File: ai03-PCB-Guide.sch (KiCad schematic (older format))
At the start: 4 parts

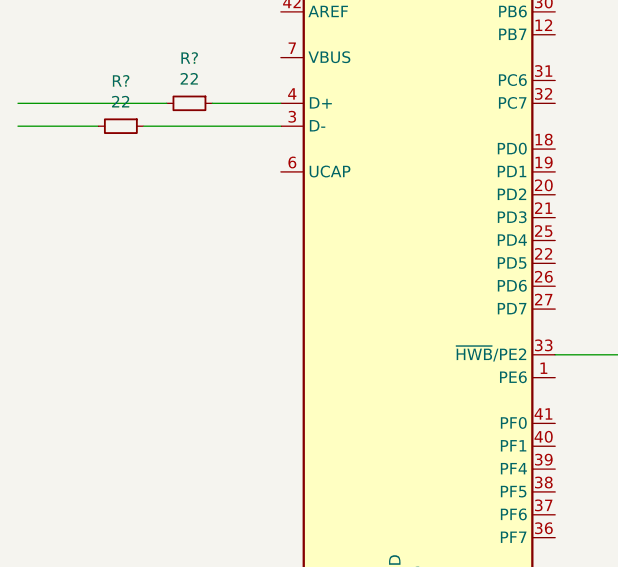
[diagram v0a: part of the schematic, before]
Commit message: New Capacitor
Added the first capacitor to the board. Done by following the official documentation and the tutorial. Generally speaking it's good if you can find the official documentation and some form of proven use case provided by another production team. (In this case, TEENSY)
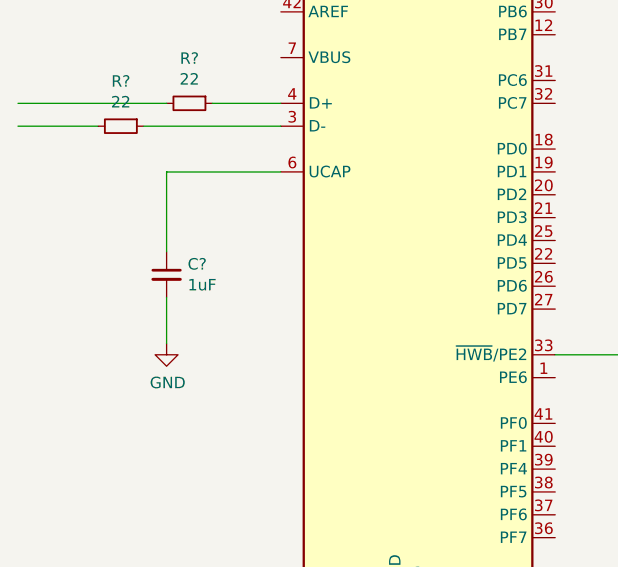
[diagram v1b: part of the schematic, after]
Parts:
- added C?: 1uF, symbol Device:C_Small
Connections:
- wire segments 11 -> 14
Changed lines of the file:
@@
 Wire Wire Line
 	2050 3100 1400 3100
+$Comp
+L Device:C_Small C?
+U 1 1 5EEF2142
+P 2050 3850
+F 0 "C?" H 2142 3896 50  0000 L CNN
+F 1 "1uF" H 2142 3805 50  0000 L CNN
+F 2 "" H 2050 3850 50  0001 C CNN
+F 3 "~" H 2050 3850 50  0001 C CNN
+	1    2050 3850
+	1    0    0    -1
+$EndComp
+Wire Wire Line
+	2550 3400 2050 3400
+Wire Wire Line
+	2050 3400 2050 3750
+$Comp
+L power:GND #PWR?
+U 1 1 5EEF42F1
+P 2050 4150
+F 0 "#PWR?" H 2050 3900 50  0001 C CNN
+F 1 "GND" H 2055 3977 50  0000 C CNN
+F 2 "" H 2050 4150 50  0001 C CNN
+F 3 "" H 2050 4150 50  0001 C CNN
+	1    2050 4150
+	1    0    0    -1
+$EndComp
+Wire Wire Line
+	2050 4150 2050 3950
 $EndSCHEMATC

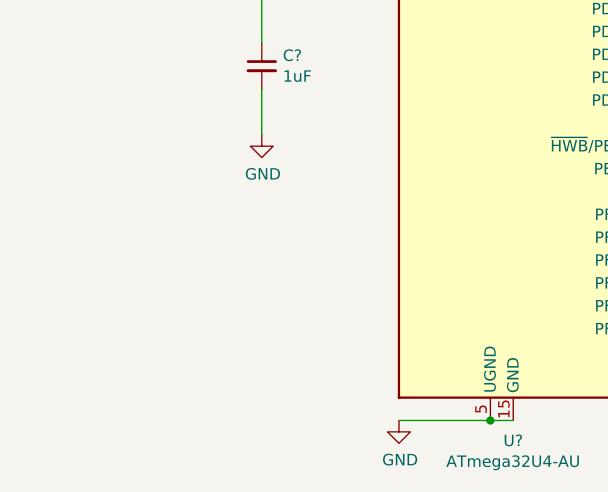
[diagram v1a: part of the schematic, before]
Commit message: Decoupling Capacitors
This step involved making the capacitors that filter the electrical noise from the microcrontroller. The official documentation says to use 0.1uF by each VCC, which would make 4, and a 10uF overall. But when looking at the Teensy Schematic, it uses 3 0.1uF and 1 1uF. The guide says to combine both, and it still works functionally. so that is what has been added here.
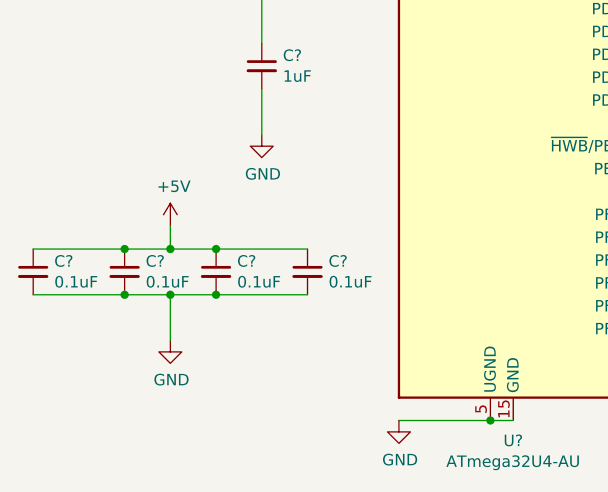
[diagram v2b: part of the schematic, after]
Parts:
- added C? (x4): 0.1uF, symbol Device:C_Small
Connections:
- wire segments 14 -> 24
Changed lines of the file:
@@
 Wire Wire Line
 	2050 4150 2050 3950
+$Comp
+L Device:C_Small C?
+U 1 1 5EEF5F01
+P 1050 4750
+F 0 "C?" H 1142 4796 50  0000 L CNN
+F 1 "0.1uF" H 1142 4705 50  0000 L CNN
+F 2 "" H 1050 4750 50  0001 C CNN
+F 3 "~" H 1050 4750 50  0001 C CNN
+	1    1050 4750
+	1    0    0    -1
+$EndComp
+$Comp
+L Device:C_Small C?
+U 1 1 5EEF6CAE
+P 1450 4750
+F 0 "C?" H 1542 4796 50  0000 L CNN
+F 1 "0.1uF" H 1542 4705 50  0000 L CNN
+F 2 "" H 1450 4750 50  0001 C CNN
+F 3 "~" H 1450 4750 50  0001 C CNN
+	1    1450 4750
+	1    0    0    -1
+$EndComp
+$Comp
+L Device:C_Small C?
+U 1 1 5EEF796E
+P 1850 4750
+F 0 "C?" H 1942 4796 50  0000 L CNN
+F 1 "0.1uF" H 1942 4705 50  0000 L CNN
+F 2 "" H 1850 4750 50  0001 C CNN
+F 3 "~" H 1850 4750 50  0001 C CNN
+	1    1850 4750
+	1    0    0    -1
+$EndComp
+$Comp
+L Device:C_Small C?
+U 1 1 5EEF8927
+P 2250 4750
+F 0 "C?" H 2342 4796 50  0000 L CNN
+F 1 "0.1uF" H 2342 4705 50  0000 L CNN
+F 2 "" H 2250 4750 50  0001 C CNN
+F 3 "~" H 2250 4750 50  0001 C CNN
+	1    2250 4750
+	1    0    0    -1
+$EndComp
+$Comp
+L power:GND #PWR?
+U 1 1 5EEF9C1D
+P 1650 5050
+F 0 "#PWR?" H 1650 4800 50  0001 C CNN
+F 1 "GND" H 1655 4877 50  0000 C CNN
+F 2 "" H 1650 5050 50  0001 C CNN
+F 3 "" H 1650 5050 50  0001 C CNN
+	1    1650 5050
+	1    0    0    -1
+$EndComp
+$Comp
+L power:+5V #PWR?
+U 1 1 5EEFAA60
+P 1650 4550
+F 0 "#PWR?" H 1650 4400 50  0001 C CNN
+F 1 "+5V" H 1665 4723 50  0000 C CNN
+F 2 "" H 1650 4550 50  0001 C CNN
+F 3 "" H 1650 4550 50  0001 C CNN
+	1    1650 4550
+	1    0    0    -1
+$EndComp
+Connection ~ 1850 4650
+Connection ~ 1850 4850
+Connection ~ 1450 4650
+Connection ~ 1450 4850
+Wire Wire Line
+	1450 4850 1650 4850
+Wire Wire Line
+	1450 4650 1650 4650
+Wire Wire Line
+	1650 5050 1650 4850
+Connection ~ 1650 4850
+Wire Wire Line
+	1650 4850 1850 4850
+Wire Wire Line
+	1650 4550 1650 4650
+Connection ~ 1650 4650
+Wire Wire Line
+	1650 4650 1850 4650
+Wire Wire Line
+	1050 4650 1450 4650
+Wire Wire Line
+	1050 4850 1450 4850
+Wire Wire Line
+	1850 4850 2250 4850
+Wire Wire Line
+	1850 4650 2250 4650
 $EndSCHEMATC

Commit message: Crystals and Reset
Added the crystals and routed to GND, also added the Reset button to allow the MCU to be put into bootloader.mm
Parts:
- added C? (x2): 22pF, symbol Device:C_Small
- added SW?: SW_Push, symbol Switch:SW_Push
- added Y?: 16MHz, symbol Device:Crystal_GND24_Small
- C?: value 0.1uF -> 10uF
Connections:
- wire segments 24 -> 44
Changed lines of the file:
@@
 P 2250 4750
 F 0 "C?" H 2342 4796 50  0000 L CNN
-F 1 "0.1uF" H 2342 4705 50  0000 L CNN
+F 1 "10uF" H 2342 4705 50  0000 L CNN
 F 2 "" H 2250 4750 50  0001 C CNN
 F 3 "~" H 2250 4750 50  0001 C CNN
@@
 Wire Wire Line
 	1850 4650 2250 4650
+Wire Wire Line
+	2550 2900 1900 2900
+$Comp
+L power:+5V #PWR?
+U 1 1 5EF047D9
+P 1900 2900
+F 0 "#PWR?" H 1900 2750 50  0001 C CNN
+F 1 "+5V" H 1915 3073 50  0000 C CNN
+F 2 "" H 1900 2900 50  0001 C CNN
+F 3 "" H 1900 2900 50  0001 C CNN
+	1    1900 2900
+	1    0    0    -1
+$EndComp
+$Comp
+L Device:Crystal_GND24_Small Y?
+U 1 1 5EF054D7
+P 2100 2400
+F 0 "Y?" V 2054 2544 50  0000 L CNN
+F 1 "16MHz" V 2145 2544 50  0000 L CNN
+F 2 "" H 2100 2400 50  0001 C CNN
+F 3 "~" H 2100 2400 50  0001 C CNN
+	1    2100 2400
+	0    1    1    0
+$EndComp
+Wire Wire Line
+	2550 2300 2100 2300
+Wire Wire Line
+	2550 2500 2100 2500
+$Comp
+L Device:C_Small C?
+U 1 1 5EF072F6
+P 1700 2200
+F 0 "C?" V 1471 2200 50  0000 C CNN
+F 1 "22pF" V 1562 2200 50  0000 C CNN
+F 2 "" H 1700 2200 50  0001 C CNN
+F 3 "~" H 1700 2200 50  0001 C CNN
+	1    1700 2200
+	0    1    1    0
+$EndComp
+$Comp
+L Device:C_Small C?
+U 1 1 5EF08CB4
+P 1700 2550
+F 0 "C?" V 1471 2550 50  0000 C CNN
+F 1 "22pF" V 1562 2550 50  0000 C CNN
+F 2 "" H 1700 2550 50  0001 C CNN
+F 3 "~" H 1700 2550 50  0001 C CNN
+	1    1700 2550
+	0    1    1    0
+$EndComp
+$Comp
+L power:GND #PWR?
+U 1 1 5EF09377
+P 1550 2750
+F 0 "#PWR?" H 1550 2500 50  0001 C CNN
+F 1 "GND" H 1555 2577 50  0000 C CNN
+F 2 "" H 1550 2750 50  0001 C CNN
+F 3 "" H 1550 2750 50  0001 C CNN
+	1    1550 2750
+	1    0    0    -1
+$EndComp
+Wire Wire Line
+	2100 2300 1800 2300
+Wire Wire Line
+	1800 2300 1800 2200
+Connection ~ 2100 2300
+Wire Wire Line
+	1600 2200 1600 2550
+Wire Wire Line
+	1600 2550 1550 2550
+Wire Wire Line
+	1550 2550 1550 2700
+Connection ~ 1600 2550
+Wire Wire Line
+	1800 2550 2100 2550
+Wire Wire Line
+	2100 2550 2100 2500
+Connection ~ 2100 2500
+Wire Wire Line
+	2000 2400 1950 2400
+Wire Wire Line
+	1950 2400 1950 2600
+Wire Wire Line
+	1950 2600 2200 2600
+Wire Wire Line
+	2200 2600 2200 2400
+Wire Wire Line
+	1950 2600 1800 2600
+Wire Wire Line
+	1800 2600 1800 2700
+Wire Wire Line
+	1800 2700 1550 2700
+Connection ~ 1950 2600
+Connection ~ 1550 2700
+Wire Wire Line
+	1550 2700 1550 2750
+$Comp
+L power:GND #PWR?
+U 1 1 5EF0F3DA
+P 2050 2050
+F 0 "#PWR?" H 2050 1800 50  0001 C CNN
+F 1 "GND" H 2055 1877 50  0000 C CNN
+F 2 "" H 2050 2050 50  0001 C CNN
+F 3 "" H 2050 2050 50  0001 C CNN
+	1    2050 2050
+	1    0    0    -1
+$EndComp
+$Comp
+L Switch:SW_Push SW?
+U 1 1 5EF0FCB2
+P 2350 2100
+F 0 "SW?" H 2350 2385 50  0000 C CNN
+F 1 "SW_Push" H 2350 2294 50  0000 C CNN
+F 2 "" H 2350 2300 50  0001 C CNN
+F 3 "~" H 2350 2300 50  0001 C CNN
+	1    2350 2100
+	1    0    0    -1
+$EndComp
+Wire Wire Line
+	2050 2050 2150 2050
+Wire Wire Line
+	2150 2050 2150 2100
 $EndSCHEMATC

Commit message: AREF Pin and Nets
Added the AREF pin to the Reset. Also added pins to the USB (Ctrl+H allows for this) in order to make it so that I don't have to run wires across the entire schematic when moving past the MCU work.
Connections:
- net labels added: D+, D-
- wire segments 44 -> 49
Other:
- moved on the sheet: SW?
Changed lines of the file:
@@
 L power:GND #PWR?
 U 1 1 5EF0F3DA
-P 2050 2050
-F 0 "#PWR?" H 2050 1800 50  0001 C CNN
-F 1 "GND" H 2055 1877 50  0000 C CNN
-F 2 "" H 2050 2050 50  0001 C CNN
-F 3 "" H 2050 2050 50  0001 C CNN
-	1    2050 2050
+P 1900 2050
+F 0 "#PWR?" H 1900 1800 50  0001 C CNN
+F 1 "GND" H 1905 1877 50  0000 C CNN
+F 2 "" H 1900 2050 50  0001 C CNN
+F 3 "" H 1900 2050 50  0001 C CNN
+	1    1900 2050
 	1    0    0    -1
 $EndComp
@@
 L Switch:SW_Push SW?
 U 1 1 5EF0FCB2
-P 2350 2100
-F 0 "SW?" H 2350 2385 50  0000 C CNN
-F 1 "SW_Push" H 2350 2294 50  0000 C CNN
-F 2 "" H 2350 2300 50  0001 C CNN
-F 3 "~" H 2350 2300 50  0001 C CNN
-	1    2350 2100
+P 2250 2100
+F 0 "SW?" H 2250 2385 50  0000 C CNN
+F 1 "SW_Push" H 2250 2294 50  0000 C CNN
+F 2 "" H 2250 2300 50  0001 C CNN
+F 3 "~" H 2250 2300 50  0001 C CNN
+	1    2250 2100
 	1    0    0    -1
 $EndComp
 Wire Wire Line
-	2050 2050 2150 2050
+	2150 2050 2150 2100
 Wire Wire Line
-	2150 2050 2150 2100
+	2050 2100 2000 2100
+Wire Wire Line
+	2000 2100 2000 2050
+Wire Wire Line
+	2000 2050 1900 2050
+Wire Wire Line
+	2450 2100 2500 2100
+Wire Wire Line
+	2500 1800 2500 2100
+Connection ~ 2500 2100
+Wire Wire Line
+	2500 2100 2550 2100
+$Comp
+L power:+5V #PWR?
+U 1 1 5EF18A9D
+P 2500 1800
+F 0 "#PWR?" H 2500 1650 50  0001 C CNN
+F 1 "+5V" H 2515 1973 50  0000 C CNN
+F 2 "" H 2500 1800 50  0001 C CNN
+F 3 "" H 2500 1800 50  0001 C CNN
+	1    2500 1800
+	1    0    0    -1
+$EndComp
+Text GLabel 1400 3100 0    50   Input ~ 0
+D+
+Text GLabel 1400 3200 0    50   Input ~ 0
+D-
 $EndSCHEMATC

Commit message: USB Circuitry
Added the USB circuitry to be able to actually have an output for the board. It's not USB-C but that's covered later.
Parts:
- added F?: 500mA, symbol Device:Polyfuse_Small
- added USB?: Molex-0548190589, symbol random-keyboard-parts:Molex-0548190589
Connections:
- net labels added: VCC
- wire segments 49 -> 53
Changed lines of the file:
@@
 Text GLabel 1400 3200 0    50   Input ~ 0
 D-
+$Comp
+L Device:Polyfuse_Small F?
+U 1 1 5EF1C28D
+P 9000 1100
+F 0 "F?" V 9205 1100 50  0000 C CNN
+F 1 "500mA" V 9114 1100 50  0000 C CNN
+F 2 "" H 9050 900 50  0001 L CNN
+F 3 "~" H 9000 1100 50  0001 C CNN
+	1    9000 1100
+	0    -1   -1   0
+$EndComp
+$Comp
+L random-keyboard-parts:Molex-0548190589 USB?
+U 1 1 5EF21CB8
+P 8000 1300
+F 0 "USB?" V 8537 1267 60  0000 C CNN
+F 1 "Molex-0548190589" V 8431 1267 60  0000 C CNN
+F 2 "" H 8000 1300 60  0001 C CNN
+F 3 "" H 8000 1300 60  0001 C CNN
+	1    8000 1300
+	0    -1   -1   0
+$EndComp
+Wire Wire Line
+	8300 1100 8650 1100
+$Comp
+L power:+5V #PWR?
+U 1 1 5EF24727
+P 9500 1100
+F 0 "#PWR?" H 9500 950 50  0001 C CNN
+F 1 "+5V" H 9515 1273 50  0000 C CNN
+F 2 "" H 9500 1100 50  0001 C CNN
+F 3 "" H 9500 1100 50  0001 C CNN
+	1    9500 1100
+	1    0    0    -1
+$EndComp
+Wire Wire Line
+	9100 1100 9500 1100
+$Comp
+L power:VCC #PWR?
+U 1 1 5EF269FC
+P 8650 1100
+F 0 "#PWR?" H 8650 950 50  0001 C CNN
+F 1 "VCC" H 8665 1273 50  0000 C CNN
+F 2 "" H 8650 1100 50  0001 C CNN
+F 3 "" H 8650 1100 50  0001 C CNN
+	1    8650 1100
+	1    0    0    -1
+$EndComp
+Connection ~ 8650 1100
+Wire Wire Line
+	8650 1100 8900 1100
+Text GLabel 8300 1300 2    50   Input ~ 0
+D+
+Text GLabel 8300 1200 2    50   Input ~ 0
+D-
+$Comp
+L power:GND #PWR?
+U 1 1 5EF284FA
+P 8500 1500
+F 0 "#PWR?" H 8500 1250 50  0001 C CNN
+F 1 "GND" H 8505 1327 50  0000 C CNN
+F 2 "" H 8500 1500 50  0001 C CNN
+F 3 "" H 8500 1500 50  0001 C CNN
+	1    8500 1500
+	1    0    0    -1
+$EndComp
+Wire Wire Line
+	8300 1500 8500 1500
 $EndSCHEMATC

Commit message: Footprinting the Schematic
This is done to create the associations of the components with the actual schematic that we have made. The software can do this on it's own with smaller projects, but in future do all of this manually. Whether that be during the project or at the end of the schematic build.
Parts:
- added D1, D2, D3, D4: D_Small, Diode_SMD:D_SOD-123, symbol Device:D_Small
- added MX1, MX2, MX3, MX4: MX-NoLED, MX_Alps_Hybrid:MX-1U-NoLED, symbol MX_Alps_Hybrid:MX-NoLED
- added R4: 10k, Resistor_SMD:R_0805_2012Metric, symbol Device:R_Small
- C1, C2, C3, C4, C5, C6, C7: renamed from C?; footprint (none) -> Capacitor_SMD:C_0805_2012Metric
- F1: renamed from F?; footprint (none) -> Fuse:Fuse_1206_3216Metric
- R1, R2, R3: renamed from R?; footprint (none) -> Resistor_SMD:R_0805_2012Metric
- SW1: renamed from SW?; footprint (none) -> random-keyboard-parts:SKQG-1155865
- USB1: renamed from USB?; footprint (none) -> random-keyboard-parts:Molex-0548190589
- Y1: renamed from Y?; footprint (none) -> Crystal:Crystal_SMD_3225-4Pin_3.2x2.5mm
- gave numbers to parts that had none: 1
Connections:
- net labels added: COL0, COL1, ROW0, ROW1
- wire segments 53 -> 65
